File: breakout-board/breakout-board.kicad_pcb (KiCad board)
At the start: 2 copper layers, 5 parts, among them J1 Screw_Terminal_1x08, P0 CONN_02X25, P1 CONN_02X25

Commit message: save breakout-board from kicad 4.0
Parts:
- moved D1 39.2 mm to (148.6, 120.7), turned to 180 degrees
- moved P1 31.4 mm to (156.2, 43.2)
- moved P0 28.5 mm to (110.5, 43.2)
- moved J1 21.7 mm to (129.5, 149.9)
- moved R1 19.4 mm to (130.8, 120.7), turned to 180 degrees
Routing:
- net Net-(J1-Pad1): track 82.8 -> 0.00 mm
- net Net-(D1-Pad1): track 76.4 -> 0.00 mm
- net Net-(J1-Pad2): track 66.9 -> 0.00 mm
- net Net-(J1-Pad3): track 59.0 -> 0.00 mm
- net Net-(J1-Pad4): track 53.5 -> 0.00 mm
- net Net-(P0-Pad38): track 40.4 -> 0.00 mm
- net Net-(P0-Pad34): track 40.4 -> 0.00 mm
- net Net-(P0-Pad30): track 40.4 -> 0.00 mm
- net Net-(P0-Pad20): track 40.4 -> 0.00 mm
- net Net-(P0-Pad16): track 40.4 -> 0.00 mm
- net Net-(P0-Pad9): track 40.4 -> 0.00 mm
- net Net-(P0-Pad5): track 40.4 -> 0.00 mm
- net Net-(P0-Pad47): track 40.4 -> 0.00 mm
- net Net-(P0-Pad23): track 40.4 -> 0.00 mm
- net Net-(P0-Pad13): track 40.4 -> 0.00 mm
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
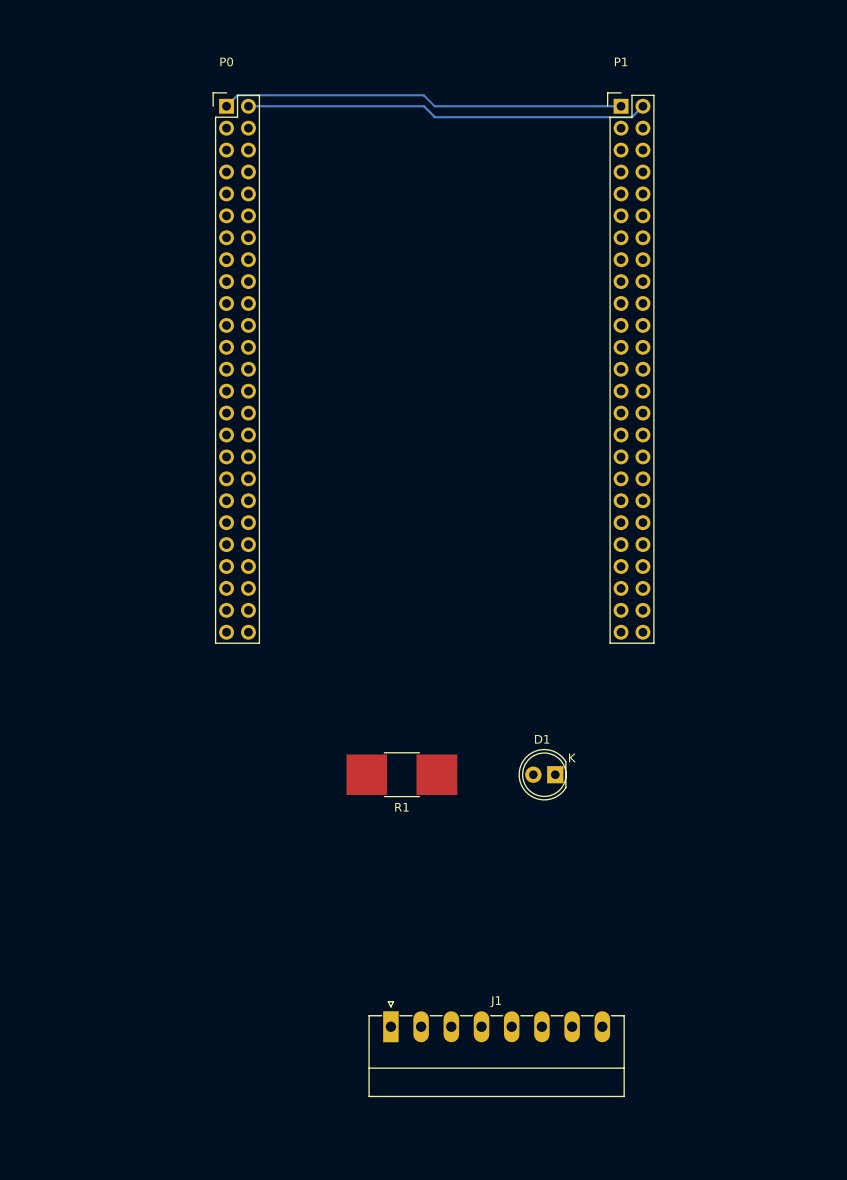
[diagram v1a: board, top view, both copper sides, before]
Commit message: update breakout board for kicad 5.0, add gerber & drill files
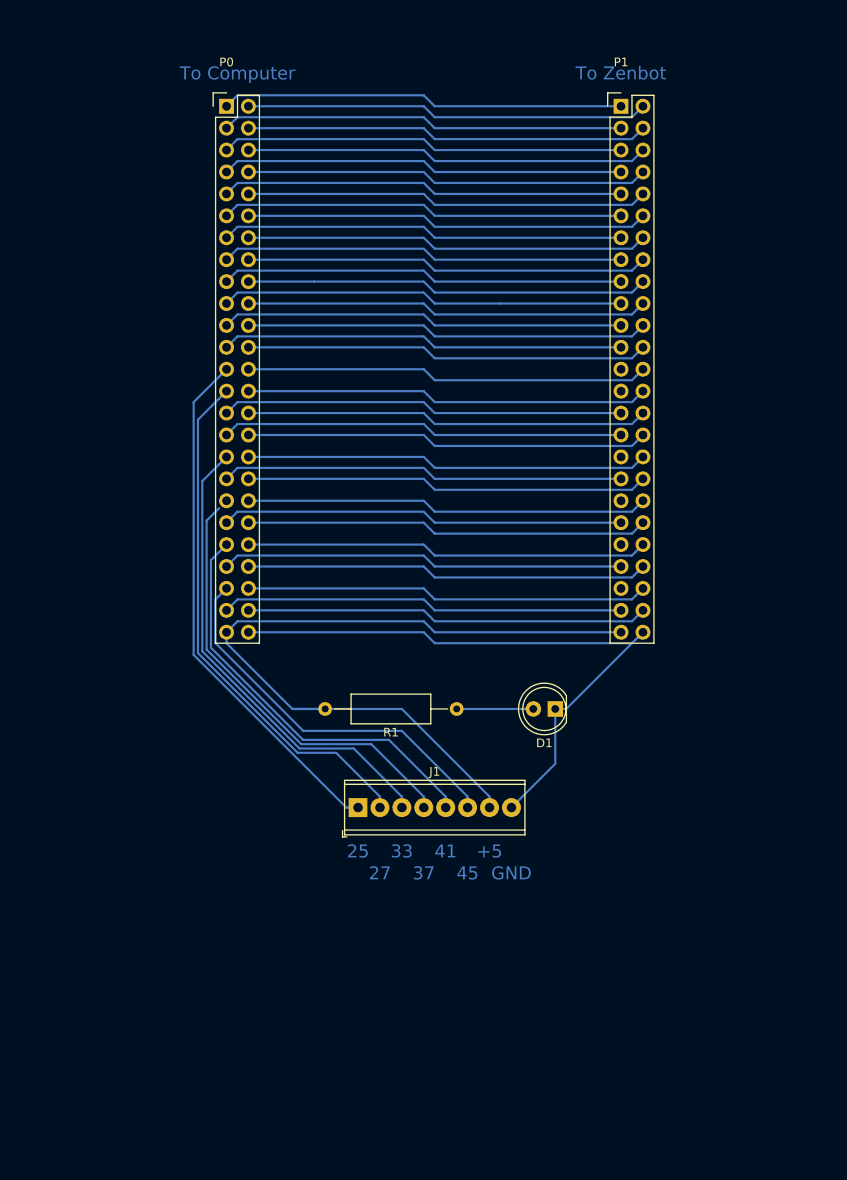
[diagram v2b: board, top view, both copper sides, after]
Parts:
- D1: footprint LEDs:LED-5MM -> LED_THT:LED_D5.0mm
- J1: footprint Connectors_Phoenix:PhoenixContact_MC-G_08x3.50mm_Angled -> TerminalBlock_Phoenix:TerminalBlock_Phoenix_MPT-0,5-8-2.54_1x08_P2.54mm_Horizontal
- R1: footprint Resistors_SMD:R_2816_HandSoldering -> Resistor_THT:R_Axial_DIN0309_L9.0mm_D3.2mm_P15.24mm_Horizontal
- moved J1 25.7 mm to (125.7, 124.5)
- moved R1 9.92 mm to (137.2, 113.0)
- moved D1 7.62 mm to (148.6, 113.0)
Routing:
- net Net-(J1-Pad7): track 0.00 -> 91.0 mm
- net Net-(D1-Pad1): track 0.00 -> 72.4 mm
- net Net-(J1-Pad1): track 0.00 -> 61.1 mm
- net Net-(J1-Pad2): track 0.00 -> 61.0 mm
- net Net-(J1-Pad3): track 0.00 -> 55.1 mm
- net Net-(J1-Pad4): track 0.00 -> 50.5 mm
- net Net-(J1-Pad5): track 0.00 -> 48.3 mm
- net Net-(P0-Pad23): track 0.00 -> 46.8 mm
- net Net-(P0-Pad19): track 0.00 -> 46.8 mm
- net Net-(P0-Pad9): track 0.00 -> 46.8 mm
- net Net-(P0-Pad17): track 0.00 -> 46.8 mm
- net Net-(P0-Pad15): track 0.00 -> 46.8 mm
- net Net-(P0-Pad13): track 0.00 -> 46.8 mm
- net Net-(P0-Pad11): track 0.00 -> 46.8 mm
- net Net-(P0-Pad48): track 0.00 -> 46.8 mm
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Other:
- net class Default: clearance 0.2 -> 0.25
- rule trace_clearance: 0.2 -> 0.25
- board text added: "+5"
- board text added: "25"
- board text added: "27"
- board text added: "33"
- board text added: "37"
- board text added: "41"
- board text added: "45"
- board text added: "GND"
- board text added: "To Computer"
- board text added: "To Zenbot"

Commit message: add proper mounting holes
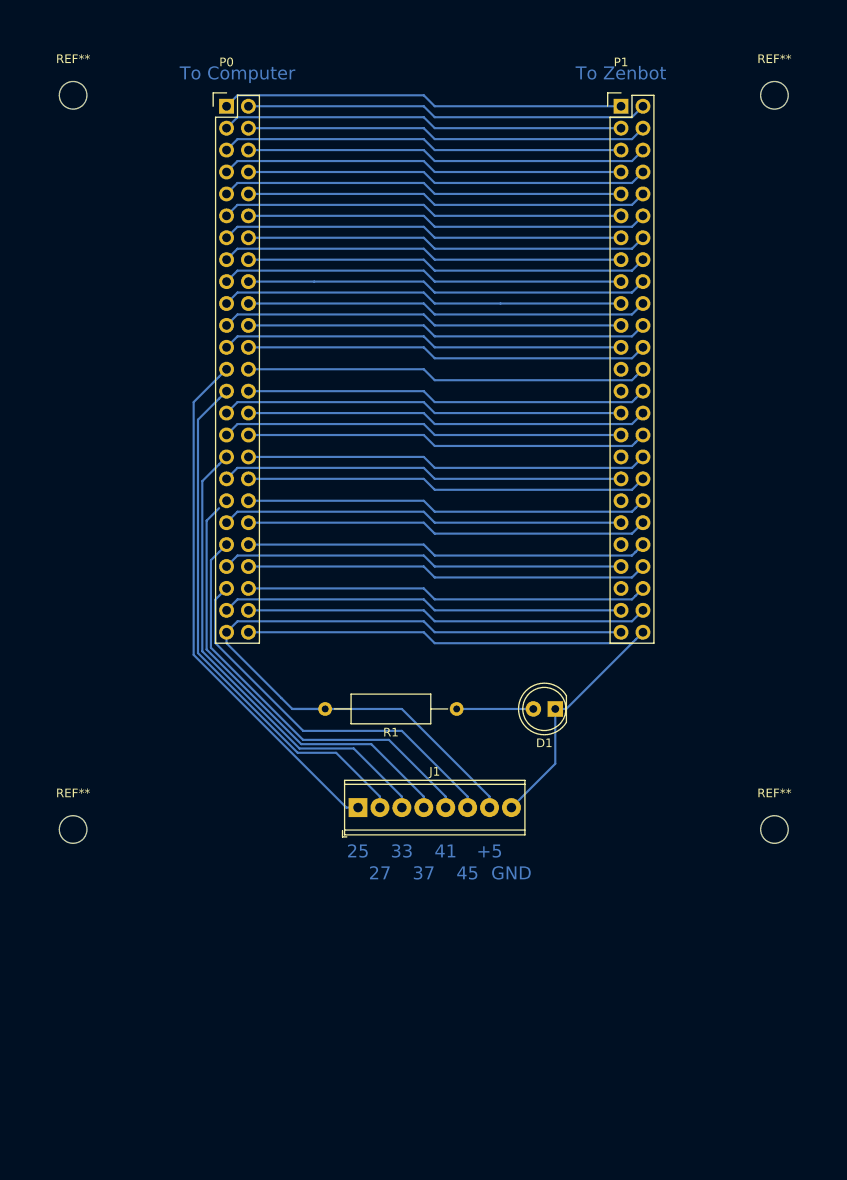
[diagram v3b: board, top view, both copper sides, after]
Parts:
- added REF**: MountingHole_3.2mm_M3, MountingHole:MountingHole_3.2mm_M3, F.Cu at (174.0, 41.9)
- added REF**: MountingHole_3.2mm_M3, MountingHole:MountingHole_3.2mm_M3, F.Cu at (92.7, 127.0)
- added REF**: MountingHole_3.2mm_M3, MountingHole:MountingHole_3.2mm_M3, F.Cu at (92.7, 41.9)
- added REF**: MountingHole_3.2mm_M3, MountingHole:MountingHole_3.2mm_M3, F.Cu at (174.0, 127.0)
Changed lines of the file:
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@@
     (tracks 238)
     (zones 0)
-    (modules 5)
+    (modules 9)
     (nets 58)
   )
@@
     )
   )
+  (module MountingHole:MountingHole_3.2mm_M3 (layer F.Cu)
+    (at 173.99 41.91)
+    (descr "Mounting Hole 3.2mm, no annular, M3")
+    (tags "mounting hole 3.2mm no annular m3")
+    (attr virtual)
+    (fp_text reference REF** (at 0 -4.2) (layer F.SilkS)
+      (effects (font (size 1 1) (thickness 0.15)))
+    )
+    (fp_text value MountingHole_3.2mm_M3 (at 0 4.2) (layer F.Fab)
+      (effects (font (size 1 1) (thickness 0.15)))
+    )
+    (fp_circle (center 0 0) (end 3.45 0) (layer F.CrtYd) (width 0.05))
+    (fp_circle (center 0 0) (end 3.2 0) (layer Cmts.User) (width 0.15))
+    (fp_text user %R (at 0.3 0) (layer F.Fab)
+      (effects (font (size 1 1) (thickness 0.15)))
+    )
+    (pad 1 np_thru_hole circle (at 0 0) (size 3.2 3.2) (drill 3.2) (layers *.Cu *.Mask))
+  )
+  (module MountingHole:MountingHole_3.2mm_M3 (layer F.Cu)
+    (at 92.71 127)
+    (descr "Mounting Hole 3.2mm, no annular, M3")
+    (tags "mounting hole 3.2mm no annular m3")
+    (attr virtual)
+    (fp_text reference REF** (at 0 -4.2) (layer F.SilkS)
+      (effects (font (size 1 1) (thickness 0.15)))
+    )
+    (fp_text value MountingHole_3.2mm_M3 (at 0 4.2) (layer F.Fab)
+      (effects (font (size 1 1) (thickness 0.15)))
+    )
+    (fp_circle (center 0 0) (end 3.45 0) (layer F.CrtYd) (width 0.05))
+    (fp_circle (center 0 0) (end 3.2 0) (layer Cmts.User) (width 0.15))
+    (fp_text user %R (at 0.3 0) (layer F.Fab)
+      (effects (font (size 1 1) (thickness 0.15)))
+    )
+    (pad 1 np_thru_hole circle (at 0 0) (size 3.2 3.2) (drill 3.2) (layers *.Cu *.Mask))
+  )
+  (module MountingHole:MountingHole_3.2mm_M3 (layer F.Cu)
+    (at 92.71 41.91)
+    (descr "Mounting Hole 3.2mm, no annular, M3")
+    (tags "mounting hole 3.2mm no annular m3")
+    (attr virtual)
+    (fp_text reference REF** (at 0 -4.2) (layer F.SilkS)
+      (effects (font (size 1 1) (thickness 0.15)))
+    )
+    (fp_text value MountingHole_3.2mm_M3 (at 0 4.2) (layer F.Fab)
+      (effects (font (size 1 1) (thickness 0.15)))
+    )
+    (fp_circle (center 0 0) (end 3.45 0) (layer F.CrtYd) (width 0.05))
+    (fp_circle (center 0 0) (end 3.2 0) (layer Cmts.User) (width 0.15))
+    (fp_text user %R (at 0.3 0) (layer F.Fab)
+      (effects (font (size 1 1) (thickness 0.15)))
+    )
+    (pad 1 np_thru_hole circle (at 0 0) (size 3.2 3.2) (drill 3.2) (layers *.Cu *.Mask))
+  )
+  (module MountingHole:MountingHole_3.2mm_M3 (layer F.Cu)
+    (at 173.99 127)
+    (descr "Mounting Hole 3.2mm, no annular, M3")
+    (tags "mounting hole 3.2mm no annular m3")
+    (attr virtual)
+    (fp_text reference REF** (at 0 -4.2) (layer F.SilkS)
+      (effects (font (size 1 1) (thickness 0.15)))
+    )
+    (fp_text value MountingHole_3.2mm_M3 (at 0 4.2) (layer F.Fab)
+      (effects (font (size 1 1) (thickness 0.15)))
+    )
+    (fp_circle (center 0 0) (end 3.45 0) (layer F.CrtYd) (width 0.05))
+    (fp_circle (center 0 0) (end 3.2 0) (layer Cmts.User) (width 0.15))
+    (fp_text user %R (at 0.3 0) (layer F.Fab)
+      (effects (font (size 1 1) (thickness 0.15)))
+    )
+    (pad 1 np_thru_hole circle (at 0 0) (size 3.2 3.2) (drill 3.2) (layers *.Cu *.Mask))
+  )
   (gr_text "To Zenbot\n" (at 156.21 39.37) (layer B.Cu)

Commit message: compactify, add edge cuts, merge all drilled holes (plated and non-plated)
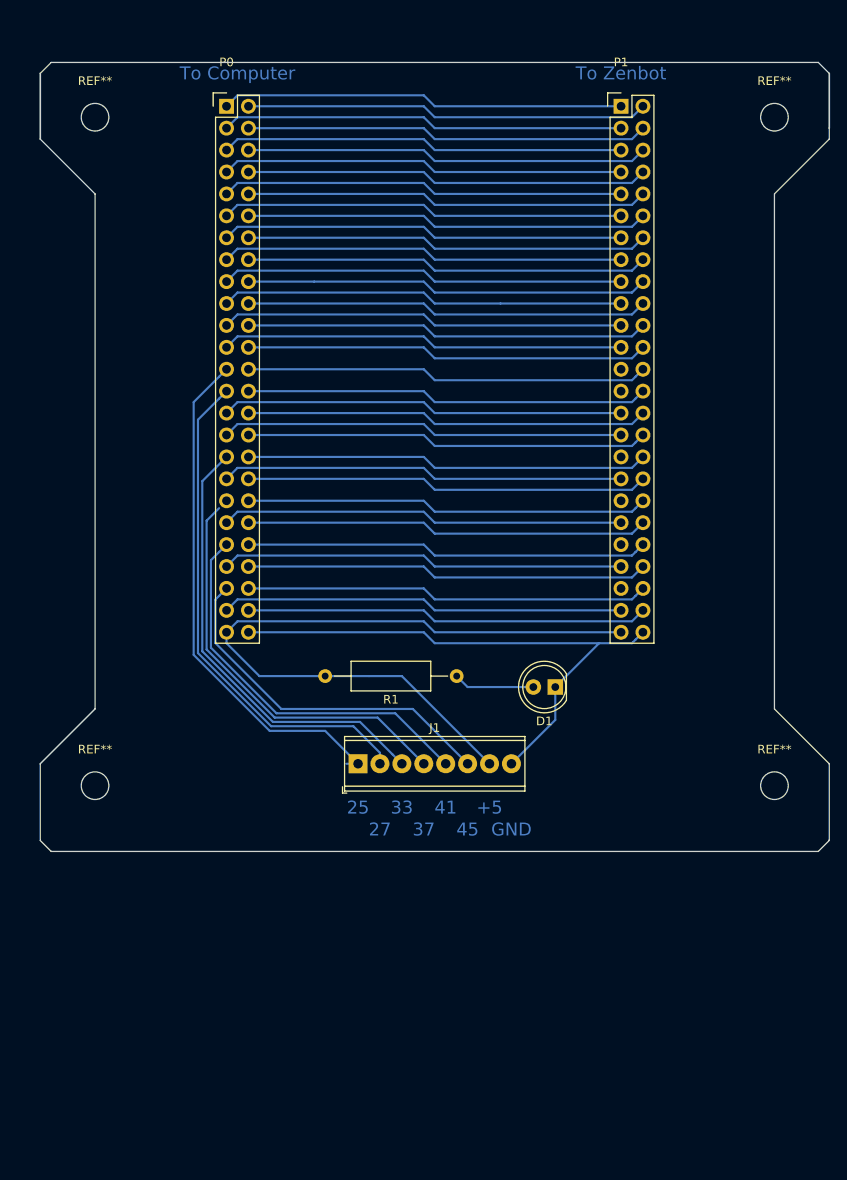
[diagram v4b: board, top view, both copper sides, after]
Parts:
- moved REF** 5.68 mm to (95.2, 121.9)
- moved J1 5.08 mm to (125.7, 119.4)
- moved REF** 5.08 mm to (174.0, 121.9)
- moved R1 3.81 mm to (137.2, 109.2)
- moved REF** 3.59 mm to (95.2, 44.5)
- moved D1 2.54 mm to (148.6, 110.5)
- moved REF** 2.54 mm to (174.0, 44.5)
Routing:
- net Net-(D1-Pad1): track 72.4 -> 65.0 mm
- net Net-(J1-Pad7): track 91.0 -> 84.3 mm
- net Net-(J1-Pad3): track 55.1 -> 52.2 mm
- net Net-(J1-Pad6): track 44.8 -> 41.9 mm
- net Net-(J1-Pad5): track 48.3 -> 45.5 mm
- net Net-(J1-Pad4): track 50.5 -> 47.6 mm
- net Net-(J1-Pad2): track 61.0 -> 58.9 mm
- net Net-(J1-Pad1): track 61.1 -> 60.3 mm
- net Net-(D1-Pad2): track 8.89 -> 9.42 mm
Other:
- board outline added: 91.4 x 91.4 mm

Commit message: breakout-board: next prototype is ready
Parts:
- removed the REF** at (174.0, 44.5)
- removed the REF** at (95.2, 121.9)
- removed the REF** at (95.2, 44.5)
- removed the REF** at (174.0, 121.9)
- added REF**: MountingHole_3.2mm_M3, MountingHole:MountingHole_3.2mm_M3, F.Cu at (102.9, 38.1)
- added REF**: MountingHole_3.2mm_M3, MountingHole:MountingHole_3.2mm_M3, F.Cu at (166.4, 38.1)
- added REF**: MountingHole_3.2mm_M3, MountingHole:MountingHole_3.2mm_M3, F.Cu at (166.4, 124.5)
- added REF**: MountingHole_3.2mm_M3, MountingHole:MountingHole_3.2mm_M3, F.Cu at (102.9, 124.5)
- P0, P1: footprint Pin_Headers:Pin_Header_Straight_2x25 -> zenbot:TE-Connectivity_1-5499923-0
- R1: footprint Resistor_THT:R_Axial_DIN0309_L9.0mm_D3.2mm_P15.24mm_Horizontal -> Resistor_THT:R_Axial_DIN0414_L11.9mm_D4.5mm_P20.32mm_Horizontal
- moved P0 63.6 mm to (113.0, 106.7), turned to 270 degrees
- moved P1 63.6 mm to (158.8, 106.7), turned to 270 degrees
- moved R1 3.01 mm to (139.9, 110.5)
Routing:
- net Net-(D1-Pad1): track 65.0 -> 60.3 mm
- net Net-(D1-Pad2): track 9.42 -> 6.16 mm
- net Net-(J1-Pad3): track 52.2 -> 54.1 mm
- net Net-(J1-Pad7): track 84.3 -> 82.5 mm
- net Net-(J1-Pad4): track 47.6 -> 49.2 mm
- net Net-(J1-Pad6): track 41.9 -> 42.5 mm
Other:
- board size 91.4 x 91.4 mm -> 73.7 x 96.5 mm

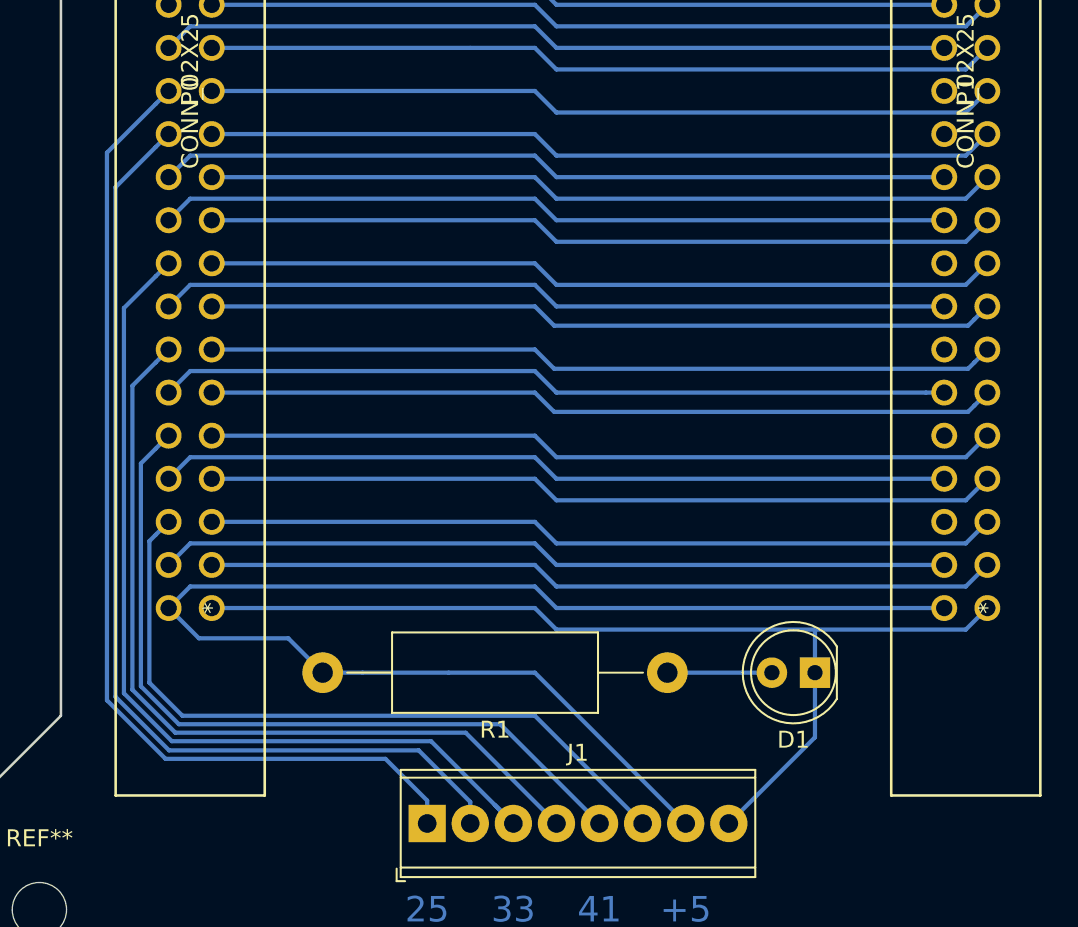
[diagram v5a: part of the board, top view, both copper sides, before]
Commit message: breakout-board: rework for lerger cutter, shallower DOC
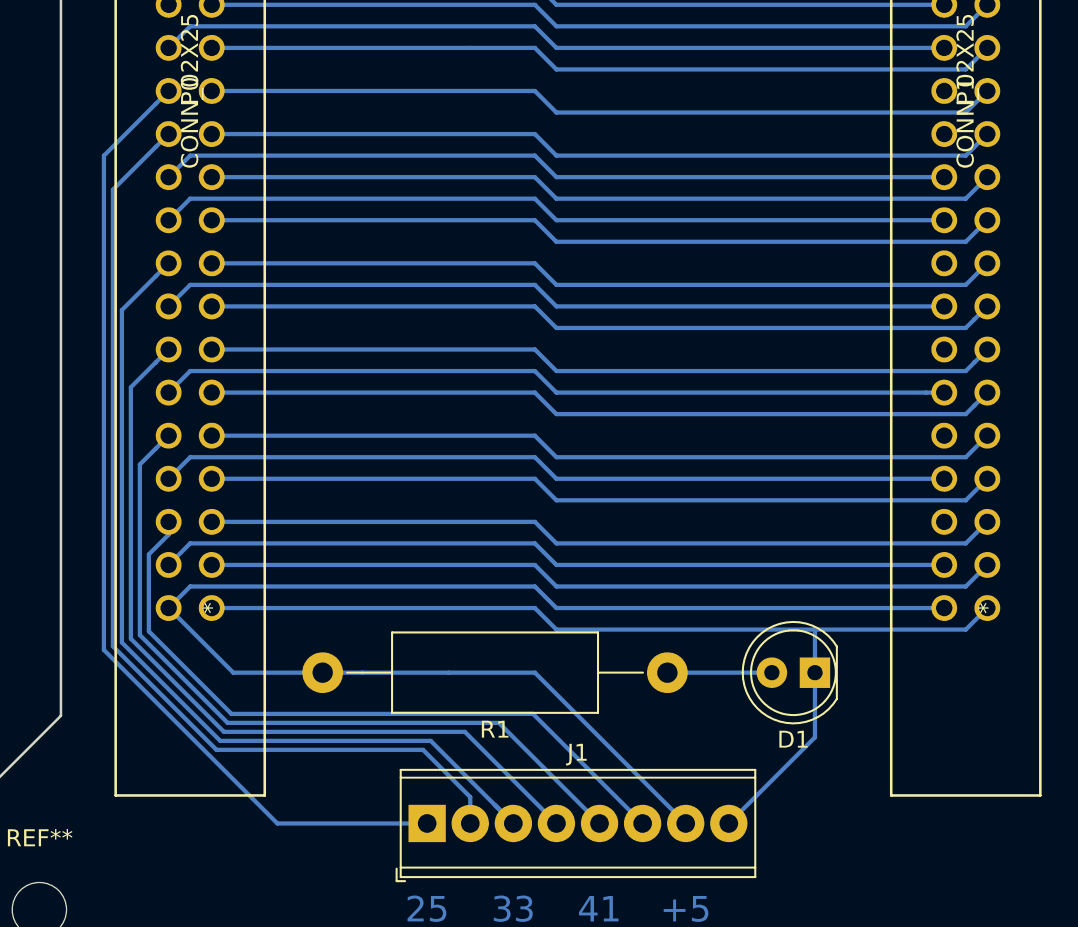
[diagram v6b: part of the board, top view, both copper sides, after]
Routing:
- net Net-(J1-Pad1): track 60.1 -> 57.8 mm
- net Net-(J1-Pad6): track 42.5 -> 40.7 mm
- net Net-(J1-Pad5): track 45.8 -> 44.2 mm
- net Net-(J1-Pad4): track 49.2 -> 47.6 mm
- net Net-(J1-Pad3): track 54.1 -> 52.5 mm
- net Net-(J1-Pad2): track 59.2 -> 57.9 mm
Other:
- net class Default: clearance 0.25 -> 0.28
- rule trace_clearance: 0.25 -> 0.28
- rule trace_min: 0.2 -> 0.25
